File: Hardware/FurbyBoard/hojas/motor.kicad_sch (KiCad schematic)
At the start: 32 parts, among them J4 Motor, U5 TPS61089RNRR, U6 DRV8231ADSGR

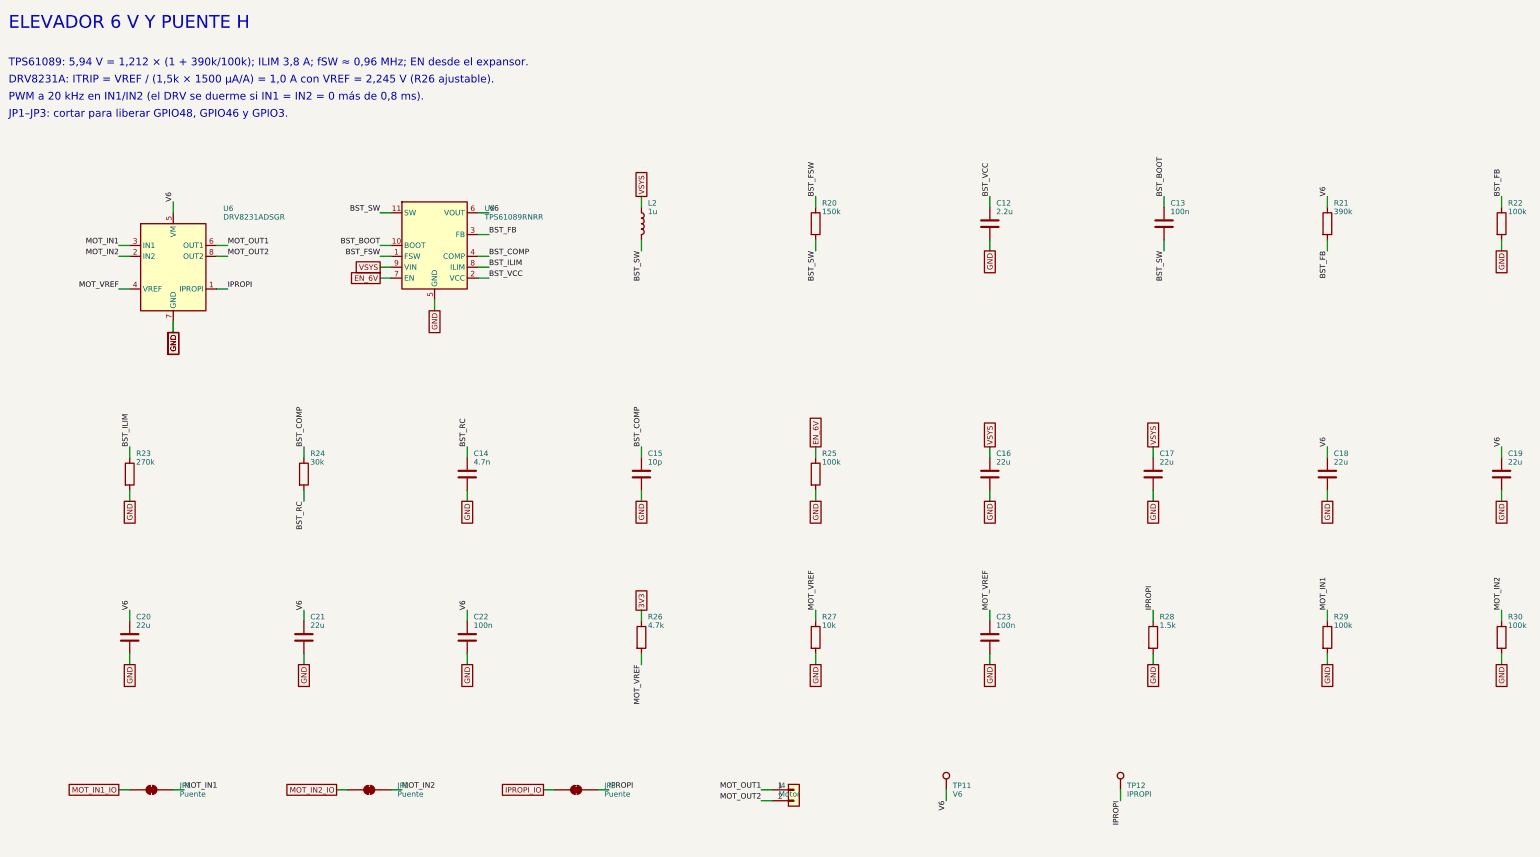
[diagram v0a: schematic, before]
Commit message: Refactor: pads de cable agrupados por zona y etiquetas globales
- Motor en J9 con leva, encoder y sensores; altavoz en J8 con inclinación y
  lengua; luz en J7 con el IR. Desaparecen J4 y J10: cada grupo sale por el
  borde más cercano a su destino.
- Micro en 2x03 en vez de 1x06 para que quepa junto al borde derecho.
- Todas las etiquetas del esquemático son globales, así el nombre de red
  coincide con el del PCB (paridad sin prefijos de hoja).
- ERC 0 errores, 0 avisos.

Co-Authored-By: Claude Opus 5.5 (1M context) <noreply@anthropic.com>
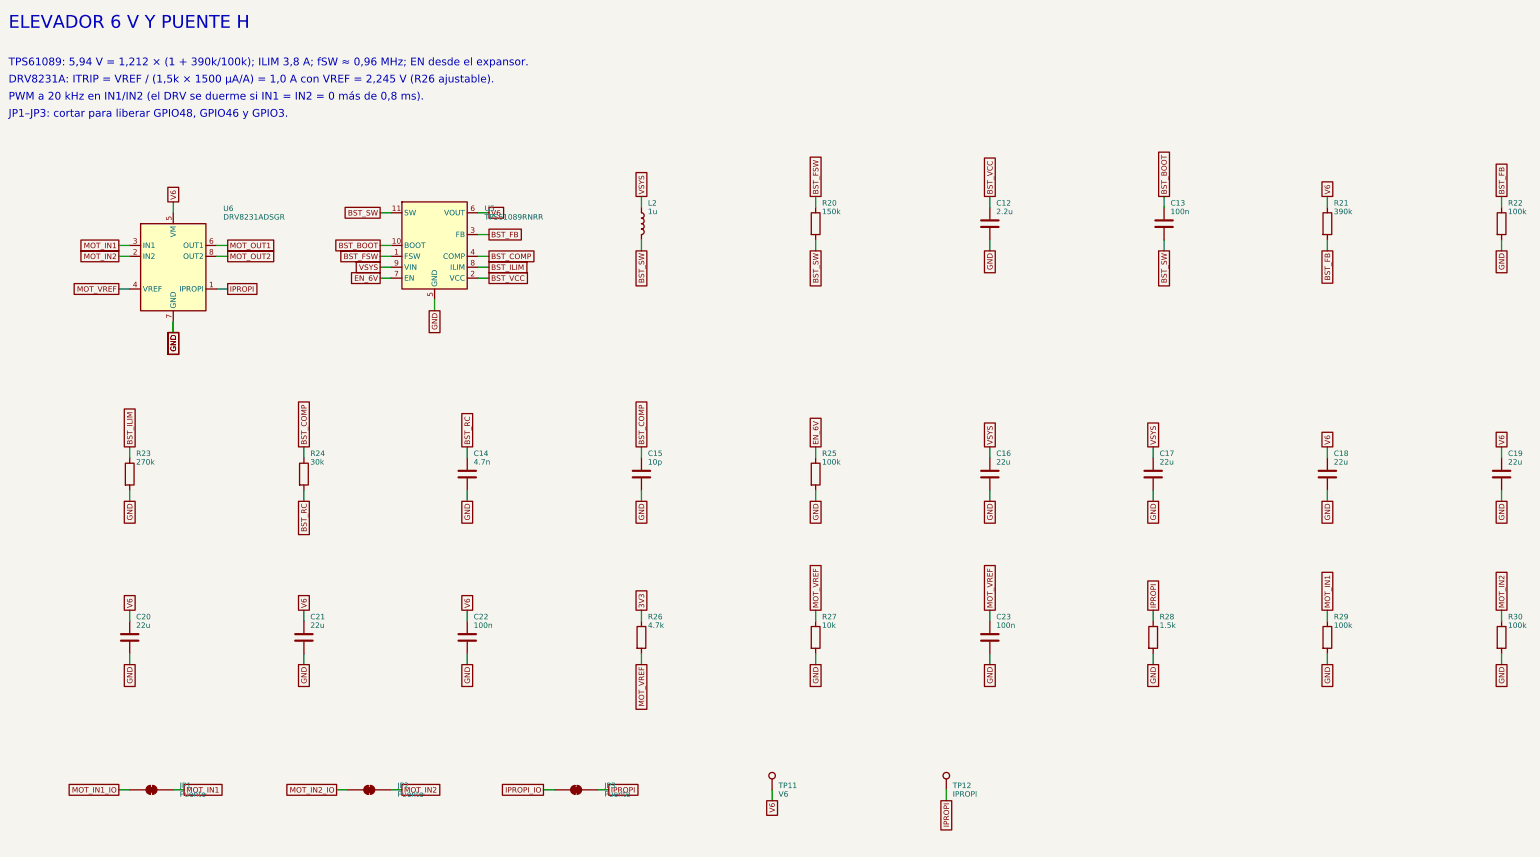
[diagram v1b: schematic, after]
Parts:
- removed J4: Motor, FurbyBoard:Pads_1x02_P2.54mm, symbol Connector_Generic:Conn_01x02
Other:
- moved on the sheet: TP11, TP12

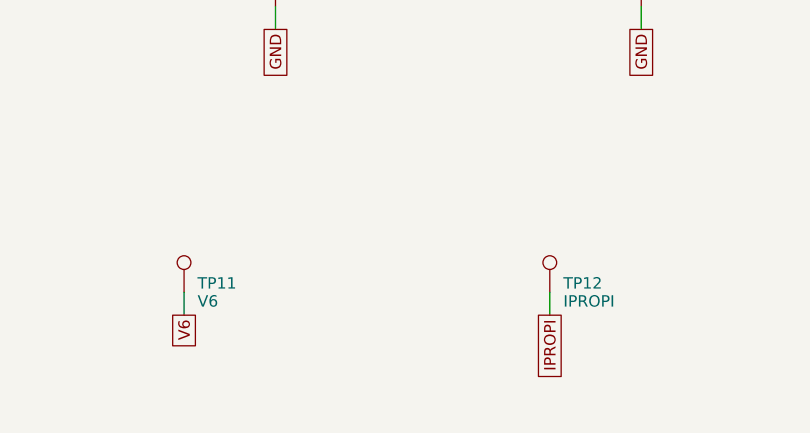
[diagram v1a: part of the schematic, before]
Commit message: Feature: par USB trazado, planos GND/VSYS y serigrafía de la FurbyBoard
- Par USB de J1 al ESD y al módulo, acoplado 0,28/0,15 por F.Cu sobre el
  plano de GND, sin vías (rutas_fijas.py, bloqueado para el autorrutado).
  Canal libre en x -83 bajo la batería.
- In1 plano de GND e In2 plano de VSYS; potencia por pista a 0,4 (cabe en
  los pads de 0,5 de paso) y 3V3 a 0,3. exportar_dsn.py deja el DSN para
  Freerouting con las clases de red.
- Rótulos de serigrafía colocados solos (serigrafia.py): TP, LED, botones,
  puentes y polaridad de la batería arriba; función de cada pad de cable y
  GPIO del J_EXP abajo, con leyenda para J7, J9 y J5.
- Para que quepan los rótulos: fila de LED con resistencias debajo, botones
  en vertical, rejilla de TP con el rótulo debajo. Quedan 14 TP: fuera EN e
  IO0 (se miden en los pads de SW1 y SW2), CHG y PG (en D1 y D2) y un GND.

ERC 0/0. DRC 0 salvo una vía de GND sin plano relleno; sin rutar.

Co-Authored-By: Claude Opus 5.5 (1M context) <noreply@anthropic.com>
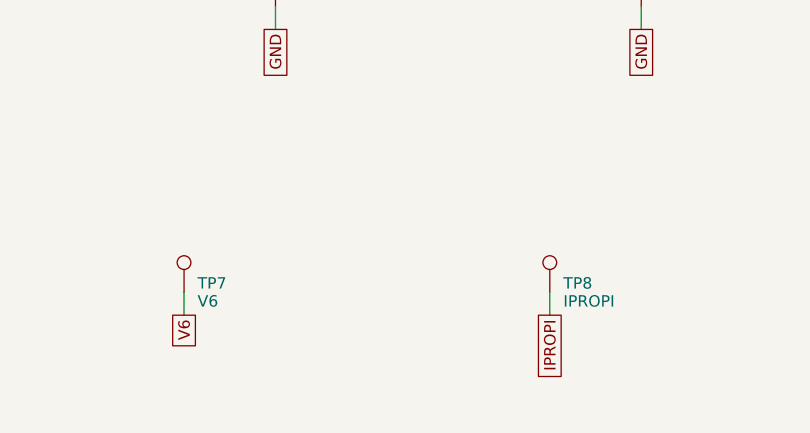
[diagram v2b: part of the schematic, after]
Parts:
- removed TP11: V6, TestPoint:TestPoint_Pad_D1.5mm, symbol Connector:TestPoint
- removed TP12: IPROPI, TestPoint:TestPoint_Pad_D1.5mm, symbol Connector:TestPoint
- added TP7: V6, TestPoint:TestPoint_Pad_D1.5mm, symbol Connector:TestPoint
- added TP8: IPROPI, TestPoint:TestPoint_Pad_D1.5mm, symbol Connector:TestPoint
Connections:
- net IPROPI: now also TP8.1
- net V6: now also TP7.1
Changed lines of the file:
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@@
-	)
-	(symbol
-		(lib_id "Connector:TestPoint")
-		(at 238.76 200.66 0)
-		(unit 1)
-		(body_style 1)
-		(exclude_from_sim no)
-		(in_bom no)
-		(on_board yes)
-		(in_pos_files yes)
-		(dnp no)
-		(property "Reference" "TP12"
-			(at 240.26 199.66 0)
-			(show_name no)
-			(do_not_autoplace no)
-			(effects
-				(font
-					(size 1.27 1.27)
-				)
-				(justify left)
-			)
-		)
-		(property "Value" "IPROPI"
-			(at 240.26 201.66 0)
-			(show_name no)
-			(do_not_autoplace no)
-			(effects
-				(font
-					(size 1.27 1.27)
-				)
-				(justify left)
-			)
-		)
-		(property "Footprint" "TestPoint:TestPoint_Pad_D1.5mm"
-			(at 238.76 200.66 0)
-			(hide yes)
-			(show_name no)
-			(do_not_autoplace no)
-			(effects
-				(font
-					(size 1.27 1.27)
-				)
-				(justify left)
-			)
-		)
-		(property "Datasheet" ""
-			(at 238.76 200.66 0)
-			(hide yes)
-			(show_name no)
-			(do_not_autoplace no)
-			(effects
-				(font
-					(size 1.27 1.27)
-				)
-				(justify left)
-			)
-		)
-		(property "Description" "2,25 V/A"
-			(at 238.76 200.66 0)
-			(hide yes)
-			(show_name no)
-			(do_not_autoplace no)
-			(effects
-				(font
-					(size 1.27 1.27)
-				)
-				(justify left)
-			)
-		)
-		(property "LCSC" ""
-			(at 238.76 200.66 0)
-			(hide yes)
-			(show_name no)
-			(do_not_autoplace no)
-			(effects
-				(font
-					(size 1.27 1.27)
-				)
-				(justify left)
-			)
-		)
-		(property "JLC_Class" ""
-			(at 238.76 200.66 0)
-			(hide yes)
-			(show_name no)
-			(do_not_autoplace no)
-			(effects
-				(font
-					(size 1.27 1.27)
-				)
-				(justify left)
-			)
-		)
-		(property "MPN" ""
-			(at 238.76 200.66 0)
-			(hide yes)
-			(show_name no)
-			(do_not_autoplace no)
-			(effects
-				(font
-					(size 1.27 1.27)
-				)
-				(justify left)
-			)
-		)
-		(pin "1"
-		)
-		(instances
-			(project "FurbyBoard"
-				(path "/8b4f1e2a-3c5d-4e6f-9a1b-2c3d4e5f6a7b/5568ca9d-1b04-5bc5-b65f-37ff2fdf9368"
-					(reference "TP12")
-					(unit 1)
-				)
-			)
-		)
 	)
 	(symbol
@@
 	)
 	(symbol
+		(lib_id "Connector:TestPoint")
+		(at 198.12 200.66 0)
+		(unit 1)
+		(body_style 1)
+		(exclude_from_sim no)
+		(in_bom no)
+		(on_board yes)
+		(in_pos_files yes)
+		(dnp no)
+		(property "Reference" "TP7"
+			(at 199.62 199.66 0)
+			(show_name no)
+			(do_not_autoplace no)
+			(effects
+				(font
+					(size 1.27 1.27)
+				)
+				(justify left)
+			)
+		)
+		(property "Value" "V6"
+			(at 199.62 201.66 0)
+			(show_name no)
+			(do_not_autoplace no)
+			(effects
+				(font
+					(size 1.27 1.27)
+				)
+				(justify left)
+			)
+		)
+		(property "Footprint" "TestPoint:TestPoint_Pad_D1.5mm"
+			(at 198.12 200.66 0)
+			(hide yes)
+			(show_name no)
+			(do_not_autoplace no)
+			(effects
+				(font
+					(size 1.27 1.27)
+				)
+				(justify left)
+			)
+		)
+		(property "Datasheet" ""
+			(at 198.12 200.66 0)
+			(hide yes)
+			(show_name no)
+			(do_not_autoplace no)
+			(effects
+				(font
+					(size 1.27 1.27)
+				)
+				(justify left)
+			)
+		)
+		(property "Description" "5,94 V con EN_6V"
+			(at 198.12 200.66 0)
+			(hide yes)
+			(show_name no)
+			(do_not_autoplace no)
+			(effects
+				(font
+					(size 1.27 1.27)
+				)
+				(justify left)
+			)
+		)
+		(property "LCSC" ""
+			(at 198.12 200.66 0)
+			(hide yes)
+			(show_name no)
+			(do_not_autoplace no)
+			(effects
+				(font
+					(size 1.27 1.27)
+				)
+				(justify left)
+			)
+		)
+		(property "JLC_Class" ""
+			(at 198.12 200.66 0)
+			(hide yes)
+			(show_name no)
+			(do_not_autoplace no)
+			(effects
+				(font
+					(size 1.27 1.27)
+				)
+				(justify left)
+			)
+		)
+		(property "MPN" ""
+			(at 198.12 200.66 0)
+			(hide yes)
+			(show_name no)
+			(do_not_autoplace no)
+			(effects
+				(font
+					(size 1.27 1.27)
+				)
+				(justify left)
+			)
+		)
+		(pin "1"
+		)
+		(instances
+			(project "FurbyBoard"
+				(path "/8b4f1e2a-3c5d-4e6f-9a1b-2c3d4e5f6a7b/5568ca9d-1b04-5bc5-b65f-37ff2fdf9368"
+					(reference "TP7")
+					(unit 1)
+				)
+			)
+		)
+	)
+	(symbol
 		(lib_id "Device:R")
 		(at 208.28 165.1 0)
@@
 	)
 	(symbol
-		(lib_id "Connector:TestPoint")
-		(at 198.12 200.66 0)
-		(unit 1)
-		(body_style 1)
-		(exclude_from_sim no)
-		(in_bom no)
-		(on_board yes)
-		(in_pos_files yes)
-		(dnp no)
-		(property "Reference" "TP11"
-			(at 199.62 199.66 0)
-			(show_name no)
-			(do_not_autoplace no)
-			(effects
-				(font
-					(size 1.27 1.27)
-				)
-				(justify left)
-			)
-		)
-		(property "Value" "V6"
-			(at 199.62 201.66 0)
-			(show_name no)
-			(do_not_autoplace no)
-			(effects
-				(font
-					(size 1.27 1.27)
-				)
-				(justify left)
-			)
-		)
-		(property "Footprint" "TestPoint:TestPoint_Pad_D1.5mm"
-			(at 198.12 200.66 0)
-			(hide yes)
-			(show_name no)
-			(do_not_autoplace no)
-			(effects
-				(font
-					(size 1.27 1.27)
-				)
-				(justify left)
-			)
-		)
-		(property "Datasheet" ""
-			(at 198.12 200.66 0)
-			(hide yes)
-			(show_name no)
-			(do_not_autoplace no)
-			(effects
-				(font
-					(size 1.27 1.27)
-				)
-				(justify left)
-			)
-		)
-		(property "Description" "5,94 V con EN_6V"
-			(at 198.12 200.66 0)
-			(hide yes)
-			(show_name no)
-			(do_not_autoplace no)
-			(effects
-				(font
-					(size 1.27 1.27)
-				)
-				(justify left)
-			)
-		)
-		(property "LCSC" ""
-			(at 198.12 200.66 0)
-			(hide yes)
-			(show_name no)
-			(do_not_autoplace no)
-			(effects
-				(font
-					(size 1.27 1.27)
-				)
-				(justify left)
-			)
-		)
-		(property "JLC_Class" ""
-			(at 198.12 200.66 0)
-			(hide yes)
-			(show_name no)
-			(do_not_autoplace no)
-			(effects
-				(font
-					(size 1.27 1.27)
-				)
-				(justify left)
-			)
-		)
-		(property "MPN" ""
-			(at 198.12 200.66 0)
-			(hide yes)
-			(show_name no)
-			(do_not_autoplace no)
-			(effects
-				(font
-					(size 1.27 1.27)
-				)
-				(justify left)
-			)
-		)
-		(pin "1"
-		)
-		(instances
-			(project "FurbyBoard"
-				(path "/8b4f1e2a-3c5d-4e6f-9a1b-2c3d4e5f6a7b/5568ca9d-1b04-5bc5-b65f-37ff2fdf9368"
-					(reference "TP11")
-					(unit 1)
-				)
-			)
-		)
-	)
-	(symbol
 		(lib_id "Device:R")
 		(at 48.26 127 0)
@@
 					(unit 1)
 				)
+			)
+		)
+	)
+	(symbol
+		(lib_id "Connector:TestPoint")
+		(at 238.76 200.66 0)
+		(unit 1)
+		(body_style 1)
+		(exclude_from_sim no)
+		(in_bom no)
+		(on_board yes)
+		(in_pos_files yes)
+		(dnp no)
+		(property "Reference" "TP8"
+			(at 240.26 199.66 0)
+			(show_name no)
+			(do_not_autoplace no)
+			(effects
+				(font
+					(size 1.27 1.27)
+				)
+				(justify left)
+			)
+		)
+		(property "Value" "IPROPI"
+			(at 240.26 201.66 0)
+			(show_name no)
+			(do_not_autoplace no)
+			(effects
+				(font
+					(size 1.27 1.27)
+				)
+				(justify left)
+			)
+		)
+		(property "Footprint" "TestPoint:TestPoint_Pad_D1.5mm"
+			(at 238.76 200.66 0)
+			(hide yes)
+			(show_name no)
+			(do_not_autoplace no)
+			(effects
+				(font
+					(size 1.27 1.27)
+				)
+				(justify left)
+			)
+		)
+		(property "Datasheet" ""
+			(at 238.76 200.66 0)
+			(hide yes)
+			(show_name no)
+			(do_not_autoplace no)
+			(effects
+				(font
+					(size 1.27 1.27)
+				)
+				(justify left)
+			)
+		)
+		(property "Description" "2,25 V/A"
+			(at 238.76 200.66 0)
+			(hide yes)
+			(show_name no)
+			(do_not_autoplace no)
+			(effects
+				(font
+					(size 1.27 1.27)
+				)
+				(justify left)
+			)
+		)
+		(property "LCSC" ""
+			(at 238.76 200.66 0)
+			(hide yes)
+			(show_name no)
+			(do_not_autoplace no)
+			(effects
+				(font
+					(size 1.27 1.27)
+				)
+				(justify left)
+			)
+		)
+		(property "JLC_Class" ""
+			(at 238.76 200.66 0)
+			(hide yes)
+			(show_name no)
+			(do_not_autoplace no)
+			(effects
+				(font
+					(size 1.27 1.27)
+				)
+				(justify left)
+			)
+		)
+		(property "MPN" ""
+			(at 238.76 200.66 0)
+			(hide yes)
+			(show_name no)
+			(do_not_autoplace no)
+			(effects
+				(font
+					(size 1.27 1.27)
+				)
+				(justify left)
+			)
+		)
+		(pin "1"
+		)
+		(instances
+			(project "FurbyBoard"
+				(path "/8b4f1e2a-3c5d-4e6f-9a1b-2c3d4e5f6a7b/5568ca9d-1b04-5bc5-b65f-37ff2fdf9368"
+					(reference "TP8")
+					(unit 1)
+				)

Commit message: Docs: notas del esquema y descripción de D5 al día con el mapa de pines final
Las notas de las hojas seguían con pines de antes del replanteo: JP1 libera
GPIO9 (no GPIO48), la INT del TCA9535 va a GPIO6 (no GPIO21), JP4 libera GPIO8
(no GPIO14) y el LED del encoder va desde V6 por 470 Ω (sin AO3400A); LED RUN en
P03 (no P16) y J_EXP 2 × 5 con el orden del bloque U. Sin cambios de redes.

Puertas: ERC 0, DRC con paridad 0/0 y 0 sin unir; cobre y rellenos idénticos.

Co-Authored-By: Claude Opus 5.5 (1M context) <noreply@anthropic.com>
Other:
- note added: "JP1–JP3: cortar para liberar GPIO9, GPIO46 y GPIO3."
- note removed: "JP1–JP3: cortar para liberar GPIO48, GPIO46 y GPIO3."
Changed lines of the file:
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@@
 		(comment 1 "Generado por scripts/gen_sch.py desde scripts/design.py: no editar a mano")
 	)
-	(text "JP1–JP3: cortar para liberar GPIO48, GPIO46 y GPIO3."
+	(text "JP1–JP3: cortar para liberar GPIO9, GPIO46 y GPIO3."
 		(exclude_from_sim no)
 		(at 20 42 0)

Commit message: Fix: M3, piezas a ≥ 0,5 mm del borde fresado: R24 en 0402 bajo C15, R23 y R50 recolocadas
Medido contra GetBoardPolygonOutlines (contorno real con el agujero del mecanismo), de borde a
borde, patio / cuerpo / pads, en las 158 huellas (script propio con pcbnew):
- R24 (30 kΩ, compensación del TPS61089): 0603 a 0,09 / 0,36 / 0,34 mm → 0402 UNI-ROYAL
  0402WGF3002TCE (C25776, extended) en (−53,88; −119,10) a 180°: 0,60 / 0,80 / 0,77 mm. En la
  esquina no hay otro hueco de 0603: la columna C12/R22/C15/R24 va a 1,6 mm de paso bajo el patio
  de L2, al oeste están C14 y el keepout de H4 y al sur la muesca del contorno. R24 sigue pegada a
  C15 (COMP) y a C14 (RC), fuera de la zona de L2 y del keepout de H4.
- R23 (ILIM): 0,30 al norte, (−45,25; −115,07): patio 0,22 → 0,40, pads 0,65 → 0,83. No cabe más:
  R50 a 0,01 al norte y las vías de VSYS de C16 (x −46,25) a 0,225 de sus pads por el oeste.
  ILIM pasa entre los pads de C16 por y −116,12 y entra en R23.1 por su eje desde el sur; la vía
  de GND de R23.2 baja a 45° al SE.
- R50 (serie de HOME): 0,15 al oeste y 0,05 al norte, (−44,65; −112,75): patio 0,41 → 0,57. La
  vía de HOME sigue en la diagonal de In2 y la columna de HOME_PAD (In2) pasa a x −43,825; la
  bajada de ENC_IO (In3) pasa de x −43,95 a −44,2 para no quedar a 0,125 de esa columna (ahora
  0,375, antes 0,275; solape 1,55 mm, por debajo del criterio de M1).
- R42 queda en 0,500 (C20 toca su patio por el oeste y R40 por el norte). J1, J7, J8, J9 y J11 son
  pads de cable o el USB-C de montaje medio, sin cuerpo: su cobre cumple los 0,3 del DRC (0,2 de
  JLCPCB); no se mueven (ver el informe).
- comprobar_colocacion.py: alturas de R_0402 (0,45) y del logo de GuilleMaker, que fallaban
  desde M7.

Puertas: ERC 0; DRC con paridad 0/0/0 (relleno de rellenar.sh); revisar-rutado 0 errores, 152
avisos (+1: entrada descentrada 0,225 en R23:1, en el eje del pad); comprobar-flujo solo los dos
cruces aceptados y los 4 desacoplos de siempre; paralelos In2/In3 19 pares, 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
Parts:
- R24: footprint Resistor_SMD:R_0603_1608Metric -> Resistor_SMD:R_0402_1005Metric; JLC_Class base -> ext; LCSC C22984 -> C25776; MPN UNI-ROYAL 0603 1% -> UNI-ROYAL 0402 1%
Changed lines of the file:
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@@
 			)
 		)
-		(property "Footprint" "Resistor_SMD:R_0603_1608Metric"
+		(property "Footprint" "Resistor_SMD:R_0402_1005Metric"
 			(at 88.9 127 0)
 			(hide yes)
@@
 			)
 		)
-		(property "LCSC" "C22984"
+		(property "LCSC" "C25776"
 			(at 88.9 127 0)
 			(hide yes)
@@
 			)
 		)
-		(property "JLC_Class" "base"
+		(property "JLC_Class" "ext"
 			(at 88.9 127 0)
 			(hide yes)
@@
 			)
 		)
-		(property "MPN" "UNI-ROYAL 0603 1%"
+		(property "MPN" "UNI-ROYAL 0402 1%"
 			(at 88.9 127 0)
 			(hide yes)
